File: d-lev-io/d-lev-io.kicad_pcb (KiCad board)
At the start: 2 copper layers, 0 parts

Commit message: more minor pusharounds and updates
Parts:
- added C1: 1u, Capacitor_SMD:C_0603_1608Metric, F.Cu at (119.0, 106.1)
- added C2: 1u, Capacitor_SMD:C_0603_1608Metric, F.Cu at (119.0, 108.6)
- added C3: 22p, Capacitor_SMD:C_0603_1608Metric, F.Cu at (119.0, 111.2)
- added C4: 22p, Capacitor_SMD:C_0603_1608Metric, F.Cu at (119.0, 113.7)
- added C5: .1u, Capacitor_SMD:C_0603_1608Metric, F.Cu at (119.0, 116.2)
- added D1: 1N914WT, Diode_SMD:D_SOD-523, F.Cu at (105.1, 100.7)
- added J1: PJ-059A, theremin:BarrelJack_CUI_PJ-059A, F.Cu at (123.6, 86.2)
- added J2: USB_C_Receptacle_USB2.0, Connector_USB:USB_C_Receptacle_HRO_TYPE-C-31-M-12, F.Cu at (81.9, 76.4)
- added J3: MIDI_OUT_JACK, Connector_Audio:Jack_3.5mm_CUI_SJ-3523-SMT_Horizontal, F.Cu at (95.0, 82.0)
- added J5: AudioJack3, Connector_Audio:Jack_3.5mm_CUI_SJ-3523-SMT_Horizontal, F.Cu at (108.9, 82.4)
- added J8: Conn_01x12_MountingPin, theremin:JST_PH_S12B-PH-SM4-TB_1x12-1MP_P2.00mm_Horizontal, F.Cu at (132.2, 78.5)
- added R1: 5.1k, Resistor_SMD:R_0805_2012Metric_Pad1.20x1.40mm_HandSolder, F.Cu at (132.5, 85.6)
- added R10: 220, Resistor_SMD:R_0603_1608Metric, F.Cu at (132.1, 97.2)
- added R2: 5.1k, Resistor_SMD:R_0805_2012Metric_Pad1.20x1.40mm_HandSolder, F.Cu at (132.5, 88.6)
- added R3: 280, Resistor_SMD:R_0603_1608Metric, F.Cu at (105.3, 93.2)
- added R4: 220, Resistor_SMD:R_0603_1608Metric, F.Cu at (105.3, 95.7)
- added R5: 10k, Resistor_SMD:R_0603_1608Metric, F.Cu at (105.3, 98.2)
- added R6: 22, Resistor_SMD:R_0805_2012Metric_Pad1.20x1.40mm_HandSolder, F.Cu at (132.5, 91.5)
- added R7: 22, Resistor_SMD:R_0805_2012Metric_Pad1.20x1.40mm_HandSolder, F.Cu at (132.5, 94.5)
- added R8: 10k, Resistor_SMD:R_0603_1608Metric, F.Cu at (119.0, 118.7)
- added R9: 10k, Resistor_SMD:R_0603_1608Metric, F.Cu at (119.0, 121.2)
- added U1: AMS1117-5.0, Package_TO_SOT_SMD:SOT-223-3_TabPin2, F.Cu at (139.8, 98.8)
- added U2: 6N137, theremin:SOP254P1030X508-8N, F.Cu at (96.9, 97.7)
- added U4: ATmega32U4-M, Package_DFN_QFN:QFN-44-1EP_7x7mm_P0.5mm_EP5.2x5.2mm, F.Cu at (125.7, 109.5)
- added Y1: 16Mhz, Oscillator:Oscillator_SMD_Abracon_ASE-4Pin_3.2x2.5mm, F.Cu at (123.6, 116.4)

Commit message: many more changes
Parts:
- removed J8: Conn_01x12_MountingPin, theremin:JST_PH_S12B-PH-SM4-TB_1x12-1MP_P2.00mm_Horizontal
- removed R5: 10k, Resistor_SMD:R_0603_1608Metric
- removed R6, R7: 22, Resistor_SMD:R_0805_2012Metric_Pad1.20x1.40mm_HandSolder
- added C10: .1u, Capacitor_SMD:C_0603_1608Metric, F.Cu at (144.4, 109.9)
- added C11: 1u, Capacitor_SMD:C_0603_1608Metric, F.Cu at (144.4, 112.4)
- added C12: 1u, Capacitor_SMD:C_0603_1608Metric, F.Cu at (144.4, 114.9)
- added C13: 10u, Capacitor_SMD:C_1210_3225Metric, F.Cu at (98.9, 89.5)
- added C14: 0.1u, Capacitor_SMD:C_0805_2012Metric, F.Cu at (104.0, 102.8)
- added C15: 0.1u, Resistor_SMD:R_0805_2012Metric, F.Cu at (93.9, 88.8)
- added C16: 75p, Capacitor_SMD:C_0603_1608Metric, F.Cu at (108.9, 101.7)
- added C17: 22u, Capacitor_SMD:C_1210_3225Metric, F.Cu at (98.9, 93.7)
- added C18: 22u, Capacitor_SMD:C_1210_3225Metric, F.Cu at (98.9, 98.0)
- added C23: 10u, Capacitor_SMD:C_0805_2012Metric, F.Cu at (162.1, 104.8)
- added C24: .1u, Capacitor_SMD:C_0603_1608Metric, F.Cu at (157.9, 104.5)
- added C25: 10u, Capacitor_SMD:C_0805_2012Metric, F.Cu at (162.1, 107.8)
- added C26: 1u, Capacitor_SMD:C_0603_1608Metric, F.Cu at (157.9, 107.0)
- added C27: .1u, Capacitor_SMD:C_0603_1608Metric, F.Cu at (157.9, 109.6)
- added C6: 10u, Capacitor_SMD:C_0805_2012Metric, F.Cu at (128.1, 104.8)
- added C7: 10u, Capacitor_SMD:C_0805_2012Metric, F.Cu at (128.1, 107.8)
- added C8: 22p, Capacitor_SMD:C_0603_1608Metric, F.Cu at (144.4, 104.8)
- added C9: 22p, Capacitor_SMD:C_0603_1608Metric, F.Cu at (144.4, 107.3)
- added D2: SS34FA, Diode_SMD:D_SOD-123F, F.Cu at (120.4, 100.8)
- added FB1: 50mohm DCR, 120R@100Mhz, Inductor_SMD:L_0603_1608Metric, F.Cu at (119.6, 103.7)
- added J4: MIDI_OUT_JACK, Connector_Audio:Jack_3.5mm_CUI_SJ-3523-SMT_Horizontal, F.Cu at (178.3, 117.5)
- added JP1: Jumper_2_Bridged, Jumper:SolderJumper-2_P1.3mm_Bridged_RoundedPad1.0x1.5mm, F.Cu at (112.3, 114.0)
- added JP2: BUCK_VERSION, Jumper:SolderJumper-2_P1.3mm_Bridged_RoundedPad1.0x1.5mm, F.Cu at (109.1, 98.7)
- added L1: 15u, Inductor_SMD:L_Bourns_SRN8040TA, F.Cu at (106.8, 92.1)
- added R11: 510k, Resistor_SMD:R_0805_2012Metric, F.Cu at (93.9, 91.8)
- added R12: 105k, Resistor_SMD:R_0805_2012Metric, F.Cu at (93.9, 94.7)
- added R13: 49.9, Resistor_SMD:R_0805_2012Metric, F.Cu at (93.9, 97.7)
- added R14: 100k, Resistor_SMD:R_0805_2012Metric, F.Cu at (93.9, 100.6)
- added R15: 13.3k, Resistor_SMD:R_0805_2012Metric, F.Cu at (93.9, 103.6)
- added R18: 10, Resistor_SMD:R_0603_1608Metric, F.Cu at (170.2, 118.8)
- added TP1: VIN, TestPoint:TestPoint_Pad_D1.5mm, F.Cu at (103.8, 110.1)
- added TP2: VUSB, TestPoint:TestPoint_Pad_D1.5mm, F.Cu at (108.2, 113.4)
- added TP3: VDD, TestPoint:TestPoint_Pad_D1.5mm, F.Cu at (132.1, 93.0)
- added TP4: VSYS, TestPoint:TestPoint_Pad_D1.5mm, F.Cu at (165.1, 119.0)
- added TP5: GND, TestPoint:TestPoint_Pad_D1.5mm, F.Cu at (103.8, 113.6)
- added U6: 74AHC1G126, Package_TO_SOT_SMD:SOT-23-5, F.Cu at (169.6, 124.8)
- C1: value 1u -> 47u; footprint Capacitor_SMD:C_0603_1608Metric -> Capacitor_SMD:C_1206_3216Metric
- C2: value 1u -> 10u; footprint Capacitor_SMD:C_0603_1608Metric -> Capacitor_SMD:C_0805_2012Metric
- C3, C4: value 22p -> 10u; footprint Capacitor_SMD:C_0603_1608Metric -> Capacitor_SMD:C_0805_2012Metric
- C5: value .1u -> 10u; footprint Capacitor_SMD:C_0603_1608Metric -> Capacitor_SMD:C_0805_2012Metric
- D1: value 1N914WT -> SS34FA; footprint Diode_SMD:D_SOD-523 -> Diode_SMD:D_SOD-123F
- J1: value PJ-059A -> USB_C_Receptacle_USB2.0; footprint theremin:BarrelJack_CUI_PJ-059A -> Connector_USB:USB_C_Receptacle_HRO_TYPE-C-31-M-12
- J2: value USB_C_Receptacle_USB2.0 -> PJ-059A; footprint Connector_USB:USB_C_Receptacle_HRO_TYPE-C-31-M-12 -> theremin:BarrelJack_CUI_PJ-059A
- J3: value MIDI_OUT_JACK -> Conn_01x12_MountingPin; footprint Connector_Audio:Jack_3.5mm_CUI_SJ-3523-SMT_Horizontal -> theremin:JST_PH_S12B-PH-SM4-TB_1x12-1MP_P2.00mm_Horizontal
- J5: value AudioJack3 -> PROG_HDR; footprint Connector_Audio:Jack_3.5mm_CUI_SJ-3523-SMT_Horizontal -> Connector:Tag-Connect_TC2030-IDC-NL_2x03_P1.27mm_Vertical
- R1, R2: footprint Resistor_SMD:R_0805_2012Metric_Pad1.20x1.40mm_HandSolder -> Resistor_SMD:R_0603_1608Metric
- R10: value 220 -> 10k
- R3: value 280 -> 22
- R4: value 220 -> 22
- R8: value 10k -> 33
- U1: value AMS1117-5.0 -> ATmega32U4-M; footprint Package_TO_SOT_SMD:SOT-223-3_TabPin2 -> Package_DFN_QFN:QFN-44-1EP_7x7mm_P0.5mm_EP5.2x5.2mm
- U2: value 6N137 -> TPS54202DDC; footprint theremin:SOP254P1030X508-8N -> Package_TO_SOT_SMD:SOT-23-6
- U4: value ATmega32U4-M -> MIC5219-3.3YM5; footprint Package_DFN_QFN:QFN-44-1EP_7x7mm_P0.5mm_EP5.2x5.2mm -> Package_TO_SOT_SMD:SOT-23-5
- Y1: value 16Mhz -> 8MHz
- moved J3 58.7 mm to (152.4, 94.1), turned to 180 degrees
- moved J5 53.0 mm to (150.4, 115.4)
- moved R8 51.2 mm to (170.2, 121.3), turned to 180 degrees
- moved J2 36.6 mm to (95.5, 110.3), turned to 0 degrees
- moved J1 36.0 mm to (114.8, 121.1)
- moved U4 35.1 mm to (158.9, 120.9)
- moved Y1 33.4 mm to (156.9, 115.1)
- moved R3 33.2 mm to (122.6, 121.5)
- moved R4 33.2 mm to (122.6, 124.1)
- moved R1 32.4 mm to (122.6, 116.5)
- moved R2 32.0 mm to (122.6, 119.0)
- moved R10 25.8 mm to (144.4, 119.9)
- moved R9 25.6 mm to (144.4, 117.4)
- moved C1 20.1 mm to (103.6, 119.0), turned to -90 degrees
- moved C2 18.3 mm to (128.1, 92.7)
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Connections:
- C1 pad 1: GND -> +12V
- C1 pad 2: Net-(U4-UCAP) -> GND
- C2 pad 1: VCC -> GND
- C2 pad 2: GND -> +5V
- C3 pad 2: Net-(U4-XTAL1) -> +5V
- C4 pad 2: Net-(U4-XTAL2) -> +5V
- C5 pad 2: Net-(U4-AREF) -> +5V
- D1 pad 2: /MIDI/midi_in- -> /Buck/VOUT
- R1 pad 2: Net-(J2-CC1) -> Net-(J1-CC1)
- R10 pad 1: /MIDI/midi_out+ -> GND
- R10 pad 2: +5V -> /AVR/HWB
- R2 pad 2: Net-(J2-CC2) -> Net-(J1-CC2)
- R3 pad 1: /MIDI/midi_in -> /USB.DM
- R3 pad 2: /MIDI/midi_opto_vcc -> Net-(J1-D--PadA7)
- R4 pad 1: GND -> /USB.DP
- R4 pad 2: Net-(D1-K) -> Net-(J1-D+-PadA6)
- R8 pad 1: /AVR/ICSP.RST -> +3V3
- R8 pad 2: VCC -> Net-(J4-PadR)
- R9 pad 1: GND -> /AVR/ICSP.RST
- R9 pad 2: /AVR/HWB -> +3V3
- U1 pad 1: unconnected-(U1-GND-Pad1) -> /AVR/INT1
- U1 pad 2: unconnected-(U1-VO-Pad2) -> +3V3
- U1 pad 3: unconnected-(U1-VI-Pad3) -> /USB.DM
- U2 pad 1: unconnected-(U2-NC-Pad1) -> GND
- U2 pad 2: /MIDI/midi_in- -> Net-(U2-SW)
- U2 pad 3: Net-(D1-K) -> +12V
- U2 pad 4: (no net) -> Net-(U2-FB)
- U2 pad 5: GND -> Net-(JP2-B)
- U2 pad 6: /MIDI/midi_in -> Net-(U2-BOOT)
- U4 pad 1: /AVR/INT1 -> +5V
- U4 pad 2: VCC -> GND
- U4 pad 3: /AVR/USB.DM -> +5V
- U4 pad 4: /AVR/USB.DP -> unconnected-(U4-BP-Pad4)
- U4 pad 5: GND -> +3V3
- Y1 pad 1: Net-(U4-XTAL2) -> Net-(U1-XTAL2)
- Y1 pad 2: Net-(U4-XTAL1) -> Net-(U1-XTAL1)

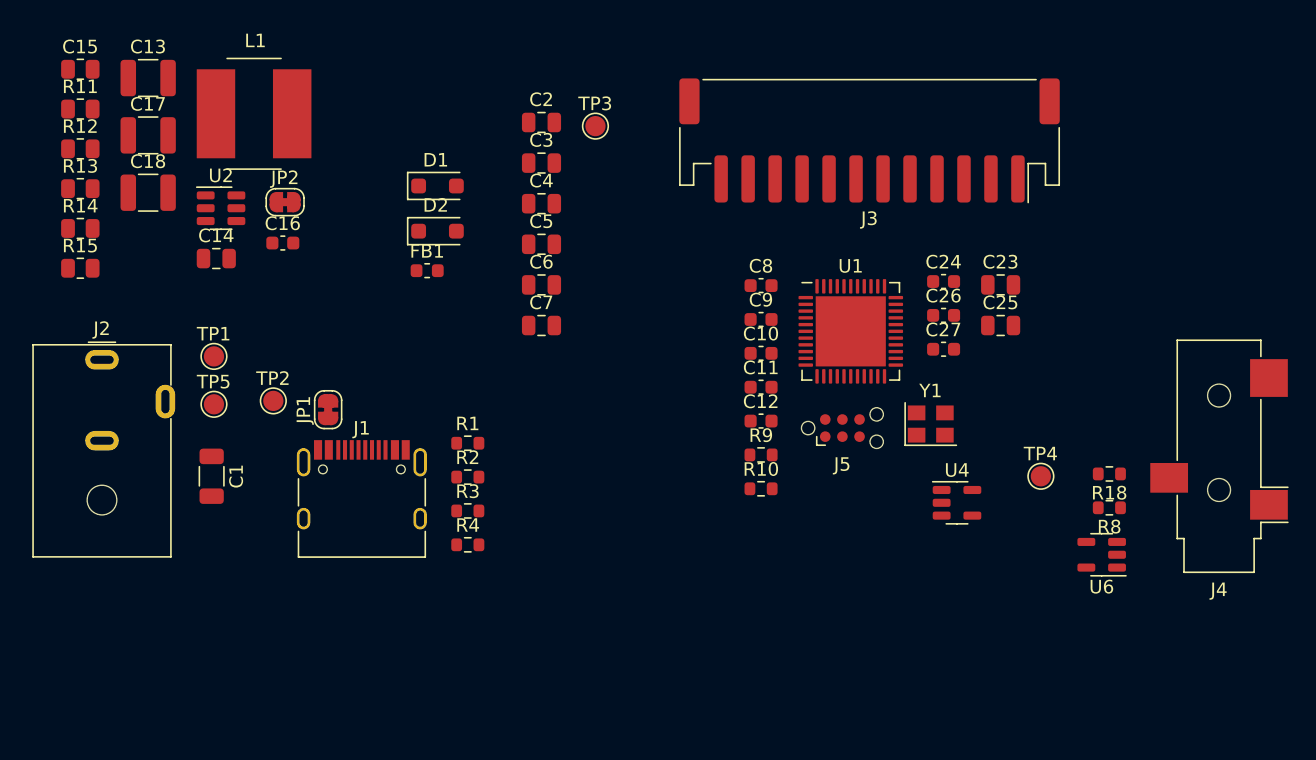
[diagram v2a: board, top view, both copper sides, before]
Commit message: map SAMD21 pins
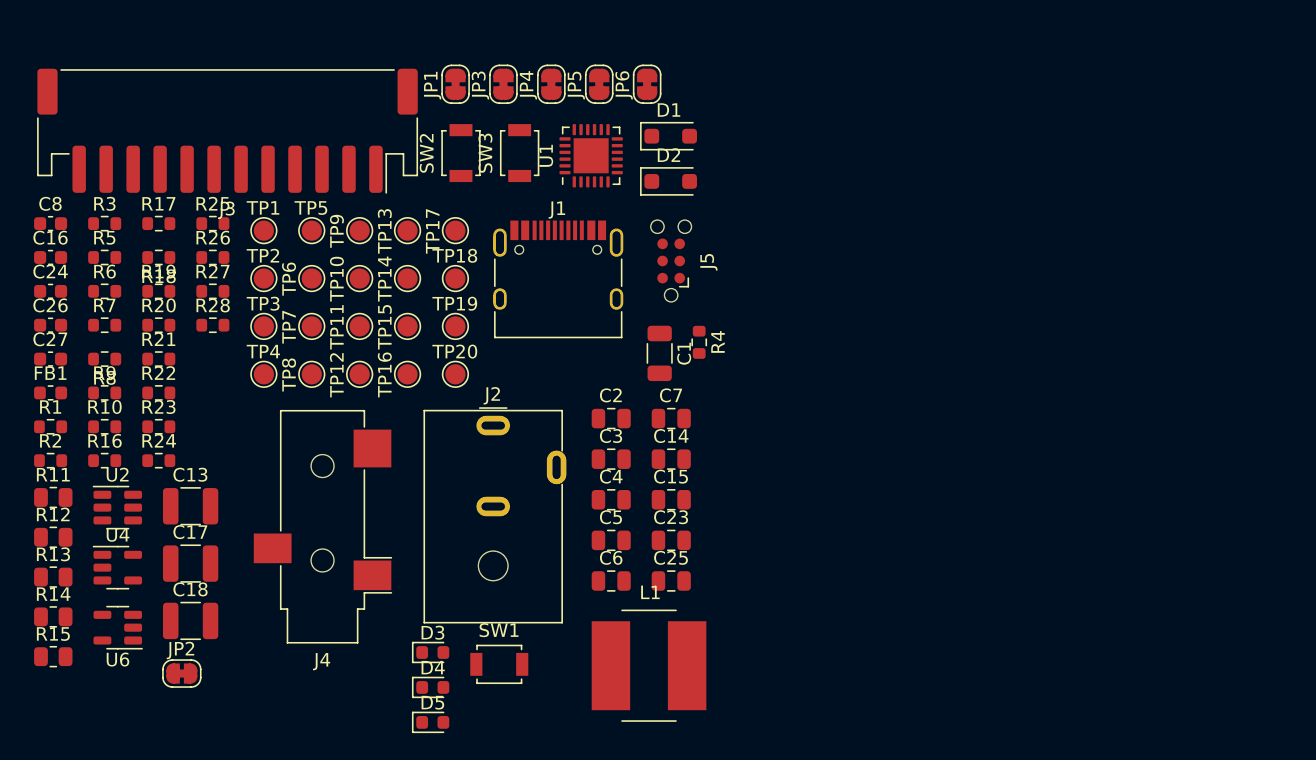
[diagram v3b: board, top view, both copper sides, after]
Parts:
- removed C10: .1u, Capacitor_SMD:C_0603_1608Metric
- removed C11, C12: 1u, Capacitor_SMD:C_0603_1608Metric
- removed C9: 22p, Capacitor_SMD:C_0603_1608Metric
- removed Y1: 8MHz, Oscillator:Oscillator_SMD_Abracon_ASE-4Pin_3.2x2.5mm
- added D3: STATUS, LED_SMD:LED_0603_1608Metric, F.Cu at (120.0, 132.0)
- added D4: LED, LED_SMD:LED_0603_1608Metric, F.Cu at (120.0, 134.6)
- added D5: STATUS_2, LED_SMD:LED_0603_1608Metric, F.Cu at (120.0, 137.2)
- added JP3: JUMP_VBUCK, Jumper:SolderJumper-2_P1.3mm_Bridged_RoundedPad1.0x1.5mm, F.Cu at (125.3, 89.9)
- added JP4: JUMP_VBUS, Jumper:SolderJumper-2_P1.3mm_Bridged_RoundedPad1.0x1.5mm, F.Cu at (128.8, 89.9)
- added JP5: ACAL_JUMPER, Jumper:SolderJumper-2_P1.3mm_Bridged_RoundedPad1.0x1.5mm, F.Cu at (132.4, 89.9)
- added JP6: MUTE_LED_JUMPER, Jumper:SolderJumper-2_P1.3mm_Bridged_RoundedPad1.0x1.5mm, F.Cu at (135.9, 89.9)
- added R16: 1k, Resistor_SMD:R_0603_1608Metric, F.Cu at (95.7, 117.8)
- added R17: 4.7k, Resistor_SMD:R_0603_1608Metric, F.Cu at (99.7, 100.2)
- added R19: 4.7k, Resistor_SMD:R_0603_1608Metric, F.Cu at (99.7, 105.3)
- added R20: 2.2k, Resistor_SMD:R_0603_1608Metric, F.Cu at (99.7, 107.8)
- added R21: 2.2k, Resistor_SMD:R_0603_1608Metric, F.Cu at (99.7, 110.3)
- added R22: 1k, Resistor_SMD:R_0603_1608Metric, F.Cu at (99.7, 112.8)
- added R23: 0, Resistor_SMD:R_0603_1608Metric, F.Cu at (99.7, 115.3)
- added R24: 0, Resistor_SMD:R_0603_1608Metric, F.Cu at (99.7, 117.8)
- added R25: 0, Resistor_SMD:R_0603_1608Metric, F.Cu at (103.7, 100.2)
- added R26: 0, Resistor_SMD:R_0603_1608Metric, F.Cu at (103.7, 102.8)
- added R27: 0, Resistor_SMD:R_0603_1608Metric, F.Cu at (103.7, 105.3)
- added R28: 1k, Resistor_SMD:R_0603_1608Metric, F.Cu at (103.7, 107.8)
- added R5: 10k, Resistor_SMD:R_0603_1608Metric, F.Cu at (95.7, 102.8)
- added R6: 330, Resistor_SMD:R_0603_1608Metric, F.Cu at (95.7, 105.3)
- added R7: 10k, Resistor_SMD:R_0603_1608Metric, F.Cu at (95.7, 107.8)
- added SW1: SW_Push, Button_Switch_SMD:SW_SPST_B3U-1000P, F.Cu at (125.0, 132.9)
- added SW2: SW_Push, Button_Switch_SMD:SW_SPST_B3U-1000P, F.Cu at (122.1, 95.0)
- added SW3: SW_Push, Button_Switch_SMD:SW_SPST_B3U-1000P, F.Cu at (126.5, 95.0)
- added TP10: VUSB, TestPoint:TestPoint_Pad_D1.5mm, F.Cu at (114.6, 104.3)
- added TP11: VUSB, TestPoint:TestPoint_Pad_D1.5mm, F.Cu at (114.6, 107.9)
- added TP12: VUSB, TestPoint:TestPoint_Pad_D1.5mm, F.Cu at (114.6, 111.4)
- added TP13: VUSB, TestPoint:TestPoint_Pad_D1.5mm, F.Cu at (118.2, 100.8)
- added TP14: VUSB, TestPoint:TestPoint_Pad_D1.5mm, F.Cu at (118.2, 104.3)
- added TP15: VUSB, TestPoint:TestPoint_Pad_D1.5mm, F.Cu at (118.2, 107.9)
- added TP16: VUSB, TestPoint:TestPoint_Pad_D1.5mm, F.Cu at (118.2, 111.4)
- added TP17: VUSB, TestPoint:TestPoint_Pad_D1.5mm, F.Cu at (121.7, 100.8)
- added TP18: TestPoint, TestPoint:TestPoint_Pad_D1.5mm, F.Cu at (121.7, 104.3)
- added TP19: TestPoint, TestPoint:TestPoint_Pad_D1.5mm, F.Cu at (121.7, 107.9)
- added TP20: TestPoint, TestPoint:TestPoint_Pad_D1.5mm, F.Cu at (121.7, 111.4)
- added TP6: VUSB, TestPoint:TestPoint_Pad_D1.5mm, F.Cu at (111.1, 104.3)
- added TP7: VUSB, TestPoint:TestPoint_Pad_D1.5mm, F.Cu at (111.1, 107.9)
- added TP8: VUSB, TestPoint:TestPoint_Pad_D1.5mm, F.Cu at (111.1, 111.4)
- added TP9: VUSB, TestPoint:TestPoint_Pad_D1.5mm, F.Cu at (114.6, 100.8)
- C14: value 0.1u -> .1u
- C15: value 0.1u -> .1u; footprint Resistor_SMD:R_0805_2012Metric -> Capacitor_SMD:C_0805_2012Metric
- C8: value 22p -> .1u
- JP1: value Jumper_2_Bridged -> MUTE_JUMPER
- R10: value 10k -> 4.7k
- R9: value 10k -> 2.2k
- U1: value ATmega32U4-M -> ATSAMD11D14A-M; footprint Package_DFN_QFN:QFN-44-1EP_7x7mm_P0.5mm_EP5.2x5.2mm -> Package_DFN_QFN:QFN-24-1EP_4x4mm_P0.5mm_EP2.6x2.6mm
- moved R8 75.3 mm to (95.7, 110.3)
- moved U6 73.1 mm to (96.7, 130.2)
- moved R18 72.3 mm to (99.7, 102.8)
- moved J4 66.7 mm to (111.9, 122.7)
- moved C24 66.2 mm to (91.7, 105.3)
- moved C26 66.2 mm to (91.7, 107.8)
- moved C27 66.2 mm to (91.7, 110.3)
- moved U4 62.4 mm to (96.7, 125.7)
- moved TP4 58.1 mm to (107.5, 111.4)
- moved C15 54.2 mm to (137.7, 120.7)
- moved C8 52.9 mm to (91.7, 100.2)
- moved L1 50.3 mm to (136.1, 133.0)
- moved R10 48.9 mm to (95.7, 115.3)
- moved R9 48.9 mm to (95.7, 112.8)
- moved J3 47.6 mm to (104.8, 93.4)
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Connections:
- net /AVR/GPIO4 renamed /SAMD11/USB.DP
- net /AVR/INT1 renamed /SAMD11/DAC_INTERNAL
- C8 pad 2: Net-(U1-XTAL1) -> /SAMD11/~{RST}
- D2 pad 1: Net-(D1-K) -> Net-(D2-K)
- FB1 pad 1: Net-(D1-K) -> Net-(JP3-B)
- J1 pad A4: Net-(JP1-A) -> VBUS
- J1 pad A9: Net-(JP1-A) -> VBUS
- J1 pad B4: Net-(JP1-A) -> VBUS
- J1 pad B9: Net-(JP1-A) -> VBUS
- J5 pad 1: /AVR/ICSP.MISO -> +3V3
- J5 pad 2: +3V3 -> /SAMD11/JTAG.SWDIO
- J5 pad 3: /AVR/ICSP.SCK -> /SAMD11/~{RST}
- J5 pad 4: /AVR/ICSP.MOSI -> /SAMD11/JTAG.SWCLK
- J5 pad 5: /AVR/ICSP.RST -> GND
- J5 pad 6: GND -> unconnected-(J5-Pin_6-Pad6)
- JP1 pad 1: Net-(JP1-A) -> mute_btn
- JP1 pad 2: VBUS -> Net-(JP1-B)
- R10 pad 1: GND -> Net-(JP1-B)
- R10 pad 2: /AVR/HWB -> +3V3
- R9 pad 1: /AVR/ICSP.RST -> Net-(JP5-B)
- U1 pad 10: /AVR/ICSP.MOSI -> Net-(U1-PA11)
- U1 pad 11: /AVR/ICSP.MISO -> Net-(U1-PA14)
- U1 pad 12: /AVR/GPIO2 -> Net-(U1-PA15)
- U1 pad 13: /AVR/ICSP.RST -> /SAMD11/STATUS_LED
- U1 pad 14: +3V3 -> /SAMD11/STATUS_LED_2
- U1 pad 15: GND -> /SAMD11/SDA
- U1 pad 16: Net-(U1-XTAL2) -> /SAMD11/SCL
- U1 pad 17: Net-(U1-XTAL1) -> Net-(U1-PA27)
- U1 pad 18: /AVR/SCL -> /SAMD11/~{RST}
- U1 pad 19: /AVR/SDA -> /SAMD11/JTAG.SWCLK
- U1 pad 2: +3V3 -> /SAMD11/HPA_SHDN
- U1 pad 20: /AVR/GPIO3 -> /SAMD11/JTAG.SWDIO
- U1 pad 21: uart_tx_3v -> /SAMD11/USB.DM
- U1 pad 25: uart_rx_3v -> (no net)
- U1 pad 3: /USB.DM -> Net-(U1-PA04)
- U1 pad 4: /USB.DP -> Net-(U1-PA05)
- U1 pad 5: GND -> /SAMD11/ESS_SHDN
- U1 pad 6: Net-(U1-UCAP) -> /SAMD11/ESS_GPIO
- U1 pad 7: +3V3 -> uart_tx_3v
- U1 pad 8: /AVR/GPIO0 -> uart_rx_3v
- U1 pad 9: /AVR/ICSP.SCK -> Net-(U1-PA10)
